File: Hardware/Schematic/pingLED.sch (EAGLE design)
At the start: 10 parts, among them IC1 LM1117MPX-3.3, U1 V_IN

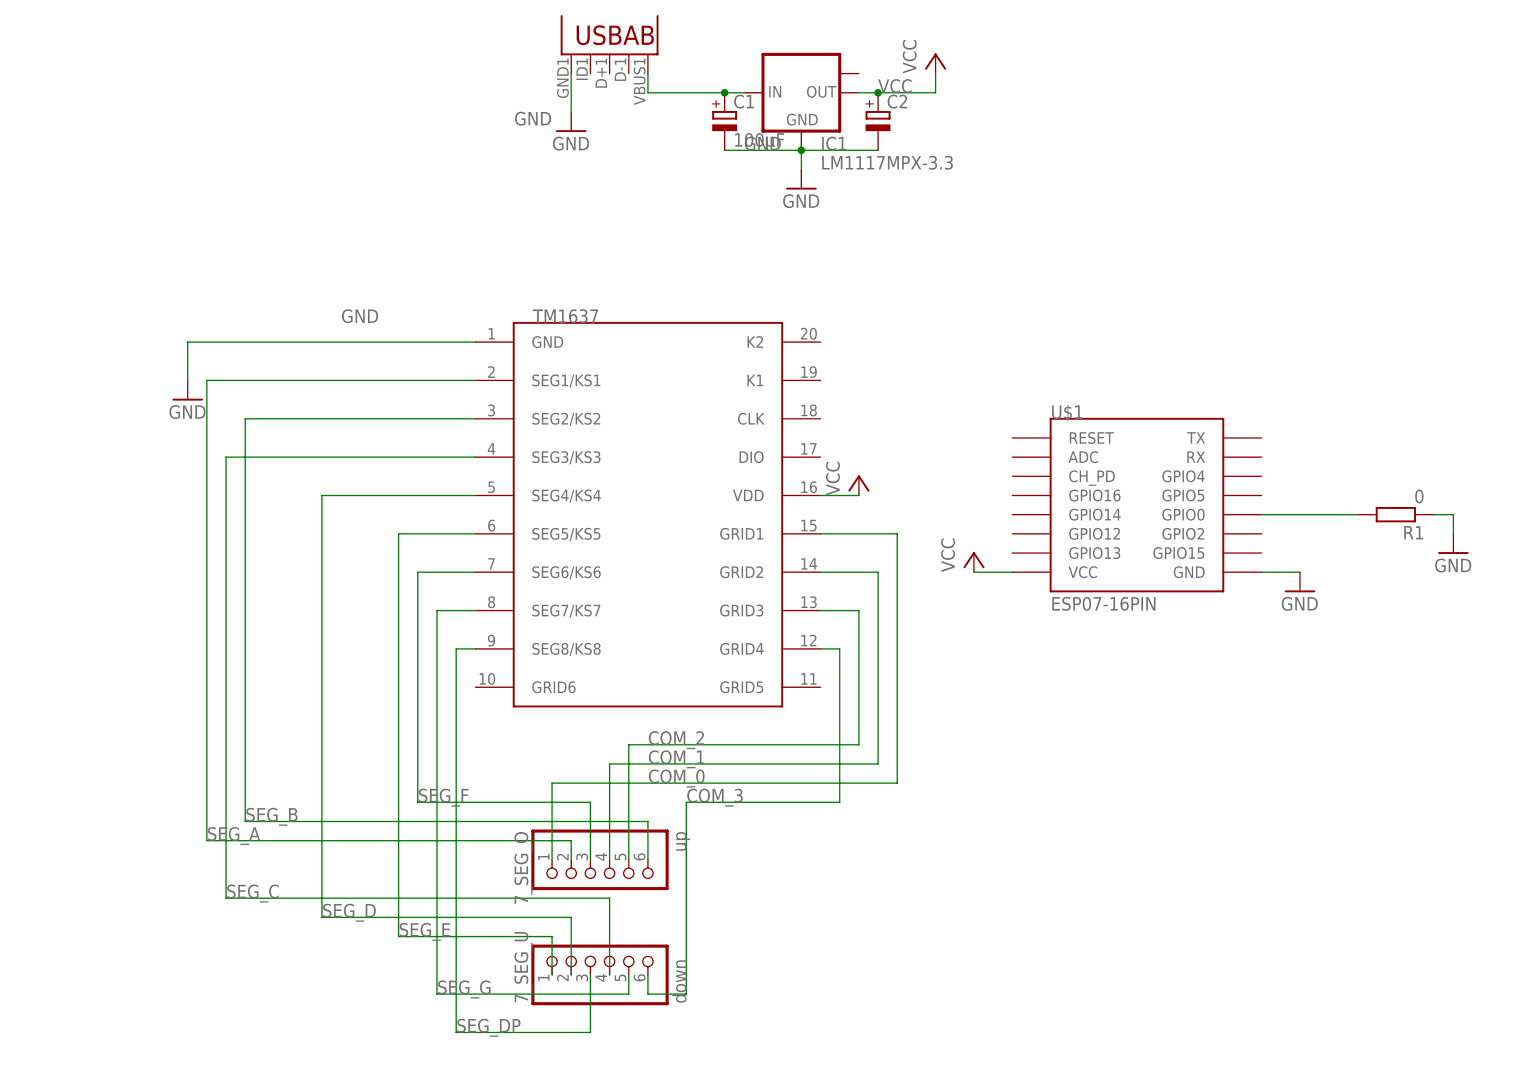
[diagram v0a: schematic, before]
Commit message: Second hardware revision done. New schematic and layout file. Cleaned up repository.
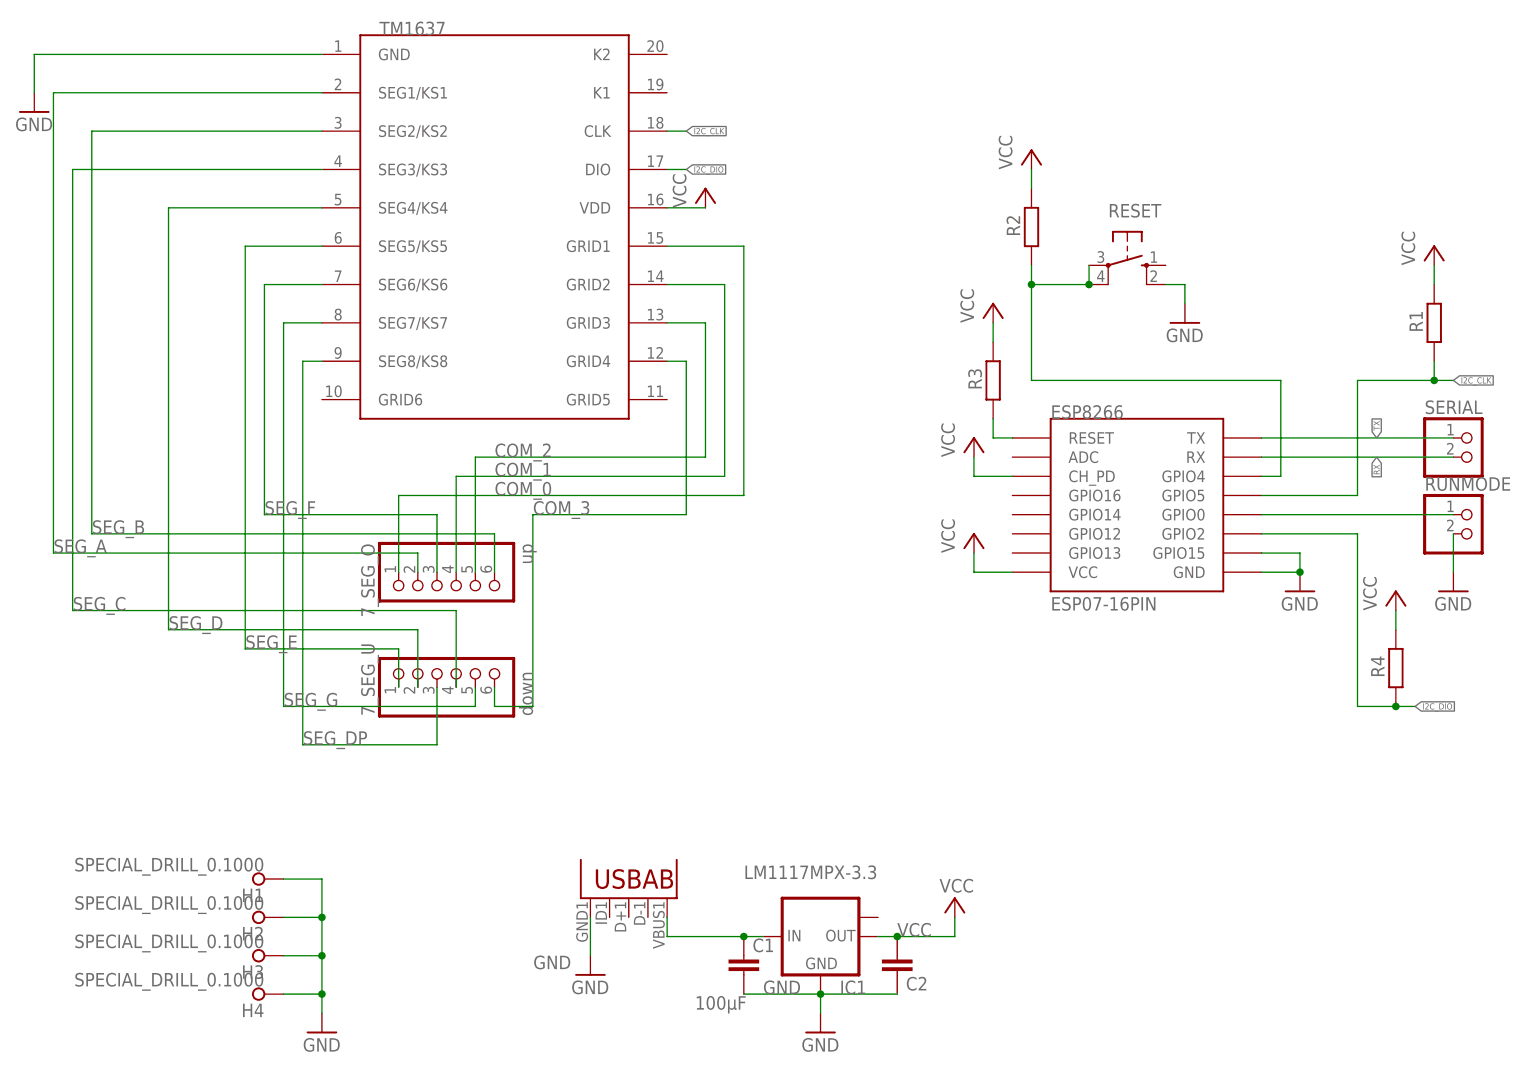
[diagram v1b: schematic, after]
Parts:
- removed U$2, U$3: TM1637SOP20, esp8266:TM1637SOP20
- added 7SEG_DRIVER: TM1637SOP20, esp8266:TM1637SOP20
- added H1, H2, H3, H4: SPECIAL_DRILL_0.1000, special-drill:SPECIAL_DRILL_0.1000
- added R2, R3, R4: (no value), rcl:R-EU_R0603
- added RESET: (no value), switch-omron:10-XX
- added RUNMODE, SERIAL: (no value), pinhead:PINHD-1X2
- C1, C2: device rcl:CPOL-EU153CLV-0505 -> rcl:C-EUC0603
- R1: value 0 -> (none)
- renumbered U$1 to ESP8266
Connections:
- new net I2C_CLK: 7SEG_DRIVER.CLK, ESP8266.GPIO5, R1.1
- new net I2C_DIO: 7SEG_DRIVER.DIO, ESP8266.GPIO2, R4.1
- new net N$2: ESP8266.GPIO4, R2.1, RESET.P, RESET.P1
- new net N$3: ESP8266.RESET, R3.1
- new net RX: ESP8266.RX, SERIAL.2
- new net TX: ESP8266.TX, SERIAL.1
- net COM_0: now also 7SEG_DRIVER.GRID1; no longer U$3.GRID1
- net COM_1: now also 7SEG_DRIVER.GRID2; no longer U$3.GRID2
- net COM_2: now also 7SEG_DRIVER.GRID3; no longer U$3.GRID3
- net COM_3: now also 7SEG_DRIVER.GRID4; no longer U$3.GRID4
- net GND: now also 7SEG_DRIVER.GND, C1.2, C2.2, ESP8266.GPIO15, H1.1, H2.1, H3.1, H4.1, RESET.S1, RUNMODE.2; no longer C1.-, C2.-, R1.1, U$3.GND
- net N$1: now also RUNMODE.1; no longer R1.2
- net N$4: now also C1.1; no longer C1.+
- net SEG_A: now also 7SEG_DRIVER.SEG1/KS1; no longer U$3.SEG1/KS1
- net SEG_B: now also 7SEG_DRIVER.SEG2/KS2; no longer U$3.SEG2/KS2
- net SEG_C: now also 7SEG_DRIVER.SEG3/KS3; no longer U$3.SEG3/KS3
- net SEG_D: now also 7SEG_DRIVER.SEG4/KS4; no longer U$3.SEG4/KS4
- net SEG_DP: now also 7SEG_DRIVER.SEG8/KS8; no longer U$3.SEG8/KS8
- net SEG_E: now also 7SEG_DRIVER.SEG5/KS5; no longer U$3.SEG5/KS5
- net SEG_F: now also 7SEG_DRIVER.SEG6/KS6; no longer U$3.SEG6/KS6
- net SEG_G: now also 7SEG_DRIVER.SEG7/KS7; no longer U$3.SEG7/KS7
- net VCC: now also 7SEG_DRIVER.VDD, C2.1, ESP8266.CH_PD, R1.2, R2.2, R3.2, R4.2; no longer C2.+, U$3.VDD
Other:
- moved on the sheet: 7_SEG_O, 7_SEG_U, IC1, R1
